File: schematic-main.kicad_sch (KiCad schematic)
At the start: 10 parts, among them J1 Conn_01x02, J2 Conn_01x03, J3 Conn_01x02, J6 Conn_01x04, P1 USB_C_Plug_USB2.0

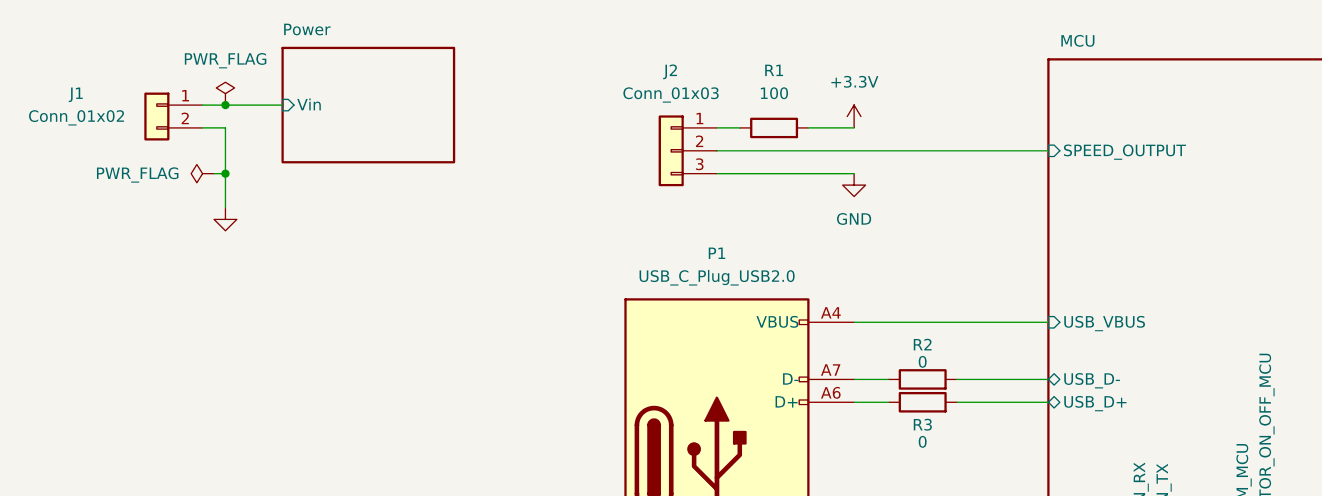
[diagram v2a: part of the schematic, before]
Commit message: Add Schottky Diode for VBUS and Vreg
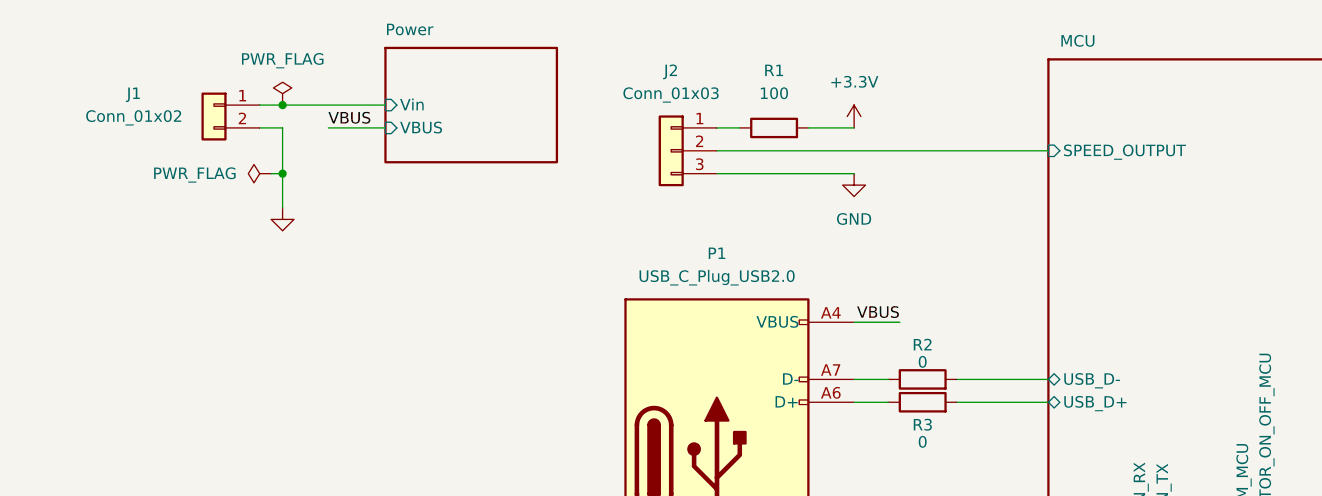
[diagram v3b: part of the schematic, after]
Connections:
- net MCU/USB_VBUS renamed VBUS
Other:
- sheet MCU ports: added none; removed USB_VBUS
- sheet Power  ports: added VBUS; removed none
- moved on the sheet: J1
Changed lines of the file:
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@@
   (junction (at 97.79 96.52) (diameter 0) (color 0 0 0 0)
   )
-  (junction (at 43.18 33.02) (diameter 0) (color 0 0 0 0)
-  )
-  (junction (at 43.18 40.64) (diameter 0) (color 0 0 0 0)
+  (junction (at 49.53 33.02) (diameter 0) (color 0 0 0 0)
+  )
+  (junction (at 49.53 40.64) (diameter 0) (color 0 0 0 0)
   )
   (junction (at 115.57 96.52) (diameter 0) (color 0 0 0 0)
@@
     (stroke (width 0) (type default))
   )
-  (wire (pts (xy 40.64 33.02) (xy 43.18 33.02))
+  (wire (pts (xy 118.11 57.15) (xy 113.03 57.15))
+    (stroke (width 0) (type default))
+  )
+  (wire (pts (xy 46.99 33.02) (xy 49.53 33.02))
     (stroke (width 0) (type default))
   )
@@
     (stroke (width 0) (type default))
   )
+  (wire (pts (xy 54.61 35.56) (xy 60.96 35.56))
+    (stroke (width 0) (type default))
+  )
   (wire (pts (xy 130.81 147.32) (xy 115.57 147.32))
     (stroke (width 0) (type default))
@@
     (stroke (width 0) (type default))
   )
-  (wire (pts (xy 43.18 40.64) (xy 43.18 44.45))
+  (wire (pts (xy 49.53 40.64) (xy 49.53 44.45))
     (stroke (width 0) (type default))
   )
@@
     (stroke (width 0) (type default))
   )
-  (wire (pts (xy 113.03 57.15) (xy 134.62 57.15))
-    (stroke (width 0) (type default))
-  )
   (wire (pts (xy 123.19 96.52) (xy 123.19 95.25))
     (stroke (width 0) (type default))
@@
     (stroke (width 0) (type default))
   )
-  (wire (pts (xy 40.64 35.56) (xy 43.18 35.56))
+  (wire (pts (xy 46.99 35.56) (xy 49.53 35.56))
     (stroke (width 0) (type default))
   )
@@
     (stroke (width 0) (type default))
   )
-  (wire (pts (xy 43.18 35.56) (xy 43.18 40.64))
+  (wire (pts (xy 49.53 35.56) (xy 49.53 40.64))
     (stroke (width 0) (type default))
   )
@@
     (stroke (width 0) (type default))
   )
-  (wire (pts (xy 43.18 33.02) (xy 49.53 33.02))
+  (wire (pts (xy 49.53 33.02) (xy 60.96 33.02))
     (stroke (width 0) (type default))
   )
@@
     (stroke (width 0) (type default))
   )
-  (wire (pts (xy 41.91 40.64) (xy 43.18 40.64))
+  (wire (pts (xy 48.26 40.64) (xy 49.53 40.64))
     (stroke (width 0) (type default))
   )
@@
   )
   (label "MOTOR_ON_OFF" (at 194.31 147.32 180) (fields_autoplaced)
+    (effects (font (size 1.27 1.27)) (justify right bottom))
+  )
+  (label "VBUS" (at 54.61 35.56 0) (fields_autoplaced)
+    (effects (font (size 1.27 1.27)) (justify left bottom))
+  )
+  (label "VBUS" (at 118.11 57.15 180) (fields_autoplaced)
     (effects (font (size 1.27 1.27)) (justify right bottom))
   )
@@
     )
   )
-  (symbol (lib_id "power:GND") (at 43.18 44.45 0) (unit 1)
-    (in_bom yes) (on_board yes) (dnp no) (fields_autoplaced)
-    (property "Reference" "#PWR03" (at 43.18 50.8 0)
-      (effects (font (size 1.27 1.27)) hide)
-    )
-    (property "Value" "GND" (at 43.18 49.53 0)
-      (effects (font (size 1.27 1.27)) hide)
-    )
-    (property "Footprint" "" (at 43.18 44.45 0)
-      (effects (font (size 1.27 1.27)) hide)
-    )
-    (property "Datasheet" "" (at 43.18 44.45 0)
+  (symbol (lib_id "power:GND") (at 49.53 44.45 0) (unit 1)
+    (in_bom yes) (on_board yes) (dnp no) (fields_autoplaced)
+    (property "Reference" "#PWR03" (at 49.53 50.8 0)
+      (effects (font (size 1.27 1.27)) hide)
+    )
+    (property "Value" "GND" (at 49.53 49.53 0)
+      (effects (font (size 1.27 1.27)) hide)
+    )
+    (property "Footprint" "" (at 49.53 44.45 0)
+      (effects (font (size 1.27 1.27)) hide)
+    )
+    (property "Datasheet" "" (at 49.53 44.45 0)
       (effects (font (size 1.27 1.27)) hide)
     )
@@
     )
   )
-  (symbol (lib_id "Connector_Generic:Conn_01x02") (at 35.56 33.02 0) (mirror y) (unit 1)
+  (symbol (lib_id "Connector_Generic:Conn_01x02") (at 41.91 33.02 0) (mirror y) (unit 1)
     (in_bom yes) (on_board yes) (dnp no)
-    (property "Reference" "J1" (at 26.67 31.75 0)
-      (effects (font (size 1.27 1.27)))
-    )
-    (property "Value" "Conn_01x02" (at 26.67 34.29 0)
-      (effects (font (size 1.27 1.27)))
-    )
-    (property "Footprint" "" (at 35.56 33.02 0)
-      (effects (font (size 1.27 1.27)) hide)
-    )
-    (property "Datasheet" "~" (at 35.56 33.02 0)
+    (property "Reference" "J1" (at 33.02 31.75 0)
+      (effects (font (size 1.27 1.27)))
+    )
+    (property "Value" "Conn_01x02" (at 33.02 34.29 0)
+      (effects (font (size 1.27 1.27)))
+    )
+    (property "Footprint" "" (at 41.91 33.02 0)
+      (effects (font (size 1.27 1.27)) hide)
+    )
+    (property "Datasheet" "~" (at 41.91 33.02 0)
       (effects (font (size 1.27 1.27)) hide)
     )
@@
       (effects (font (size 1.27 1.27)) hide)
     )
+    (pin "1")
+    (pin "2")
     (pin "3")
-    (pin "1")
     (pin "4")
-    (pin "2")
     (instances
       (project "schematic-main"
@@
     )
   )
-  (symbol (lib_id "power:PWR_FLAG") (at 41.91 40.64 90) (unit 1)
-    (in_bom yes) (on_board yes) (dnp no) (fields_autoplaced)
-    (property "Reference" "#FLG02" (at 40.005 40.64 0)
-      (effects (font (size 1.27 1.27)) hide)
-    )
-    (property "Value" "PWR_FLAG" (at 38.1 40.64 90)
-      (effects (font (size 1.27 1.27)) (justify left))
-    )
-    (property "Footprint" "" (at 41.91 40.64 0)
-      (effects (font (size 1.27 1.27)) hide)
-    )
-    (property "Datasheet" "~" (at 41.91 40.64 0)
+  (symbol (lib_id "power:PWR_FLAG") (at 48.26 40.64 90) (unit 1)
+    (in_bom yes) (on_board yes) (dnp no) (fields_autoplaced)
+    (property "Reference" "#FLG02" (at 46.355 40.64 0)
+      (effects (font (size 1.27 1.27)) hide)
+    )
+    (property "Value" "PWR_FLAG" (at 44.45 40.64 90)
+      (effects (font (size 1.27 1.27)) (justify left))
+    )
+    (property "Footprint" "" (at 48.26 40.64 0)
+      (effects (font (size 1.27 1.27)) hide)
+    )
+    (property "Datasheet" "~" (at 48.26 40.64 0)
       (effects (font (size 1.27 1.27)) hide)
     )
@@
     )
     (pin "1")
+    (pin "2")
     (pin "3")
-    (pin "2")
     (instances
       (project "schematic-main"
@@
     )
   )
-  (symbol (lib_id "power:PWR_FLAG") (at 43.18 33.02 0) (unit 1)
-    (in_bom yes) (on_board yes) (dnp no) (fields_autoplaced)
-    (property "Reference" "#FLG01" (at 43.18 31.115 0)
-      (effects (font (size 1.27 1.27)) hide)
-    )
-    (property "Value" "PWR_FLAG" (at 43.18 27.94 0)
-      (effects (font (size 1.27 1.27)))
-    )
-    (property "Footprint" "" (at 43.18 33.02 0)
-      (effects (font (size 1.27 1.27)) hide)
-    )
-    (property "Datasheet" "~" (at 43.18 33.02 0)
+  (symbol (lib_id "power:PWR_FLAG") (at 49.53 33.02 0) (unit 1)
+    (in_bom yes) (on_board yes) (dnp no) (fields_autoplaced)
+    (property "Reference" "#FLG01" (at 49.53 31.115 0)
+      (effects (font (size 1.27 1.27)) hide)
+    )
+    (property "Value" "PWR_FLAG" (at 49.53 27.94 0)
+      (effects (font (size 1.27 1.27)))
+    )
+    (property "Footprint" "" (at 49.53 33.02 0)
+      (effects (font (size 1.27 1.27)) hide)
+    )
+    (property "Datasheet" "~" (at 49.53 33.02 0)
       (effects (font (size 1.27 1.27)) hide)
     )
@@
     )
   )
-  (sheet (at 49.53 26.67) (size 19.05 12.7)
+  (sheet (at 60.96 26.67) (size 19.05 12.7)
     (stroke (width 0.254) (type solid))
     (fill (color 255 255 154 1.0000))
-    (property "Sheetname" "Power " (at 49.53 25.4 0)
+    (property "Sheetname" "Power " (at 60.96 25.4 0)
       (effects (font (size 1.27 1.27)) (justify left bottom))
     )
-    (property "Sheetfile" "schematic-power.kicad_sch" (at 50.8 47.625 0)
+    (property "Sheetfile" "schematic-power.kicad_sch" (at 62.23 47.625 0)
       (effects (font (size 1.27 1.27)) (justify left top) hide)
     )
-    (pin "Vin" input (at 49.53 33.02 180)
+    (pin "Vin" input (at 60.96 33.02 180)
+      (effects (font (size 1.27 1.27)) (justify left))
+    )
+    (pin "VBUS" input (at 60.96 35.56 180)
       (effects (font (size 1.27 1.27)) (justify left))
     )
@@
       (effects (font (size 1.27 1.27)) (justify left))
     )
-    (pin "USB_VBUS" input (at 134.62 57.15 180)
-      (effects (font (size 1.27 1.27)) (justify left))
-    )

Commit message: PCB Drawing
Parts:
- added H1, H2, H3, H4: MountingHole, MountingHole:MountingHole_2.2mm_M2, symbol Mechanical:MountingHole
- J1, J3: footprint (none) -> Connector_PinHeader_1.00mm:PinHeader_1x02_P1.00mm_Vertical
- J2: footprint (none) -> Connector_PinHeader_1.00mm:PinHeader_1x03_P1.00mm_Vertical
- J6: footprint (none) -> Connector_PinHeader_1.00mm:PinHeader_1x04_P1.00mm_Vertical
- P1: footprint (none) -> Connector_USB:2169900002
- R1, R2, R3, R4, R5: footprint (none) -> Resistor_SMD:R_1206_3216Metric
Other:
- note added: "Mounting Holes"
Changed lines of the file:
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@@
     (stroke (width 0) (type default))
+  )
+  (rectangle (start 34.29 102.87) (end 55.88 130.81)
+    (stroke (width 0) (type dash))
+    (fill (type none))
+  )
+  (text "Mounting Holes" (at 34.29 101.6 0)
+    (effects (font (size 1.7 1.7) (thickness 0.4) bold) (justify left bottom))
   )
   (label "PWM_MOTOR" (at 130.81 144.78 180) (fields_autoplaced)
@@
       (effects (font (size 1.27 1.27)))
     )
-    (property "Footprint" "" (at 101.6 72.39 0)
+    (property "Footprint" "Connector_USB:2169900002" (at 101.6 72.39 0)
       (effects (font (size 1.27 1.27)) hide)
     )
@@
       (effects (font (size 1.27 1.27)))
     )
-    (property "Footprint" "" (at 110.49 125.73 0)
+    (property "Footprint" "Connector_PinHeader_1.00mm:PinHeader_1x02_P1.00mm_Vertical" (at 110.49 125.73 0)
       (effects (font (size 1.27 1.27)) hide)
     )
@@
       (effects (font (size 1.27 1.27)))
     )
-    (property "Footprint" "" (at 41.91 33.02 0)
+    (property "Footprint" "Connector_PinHeader_1.00mm:PinHeader_1x02_P1.00mm_Vertical" (at 41.91 33.02 0)
       (effects (font (size 1.27 1.27)) hide)
     )
@@
       (effects (font (size 1.27 1.27)))
     )
-    (property "Footprint" "" (at 120.65 67.818 90)
+    (property "Footprint" "Resistor_SMD:R_1206_3216Metric" (at 120.65 67.818 90)
       (effects (font (size 1.27 1.27)) hide)
     )
@@
       (effects (font (size 1.27 1.27)))
     )
-    (property "Footprint" "" (at 110.49 144.78 0)
+    (property "Footprint" "Connector_PinHeader_1.00mm:PinHeader_1x04_P1.00mm_Vertical" (at 110.49 144.78 0)
       (effects (font (size 1.27 1.27)) hide)
     )
@@
       (effects (font (size 1.27 1.27)))
     )
-    (property "Footprint" "" (at 104.14 37.338 90)
+    (property "Footprint" "Resistor_SMD:R_1206_3216Metric" (at 104.14 37.338 90)
       (effects (font (size 1.27 1.27)) hide)
     )
@@
         (path "/c9ad7189-d3b2-414a-9743-efd8e57cd755"
           (reference "R1") (unit 1)
+        )
+      )
+    )
+  )
+  (symbol (lib_id "Mechanical:MountingHole") (at 38.1 113.03 0) (unit 1)
+    (in_bom yes) (on_board yes) (dnp no) (fields_autoplaced)
+    (property "Reference" "H2" (at 40.64 111.76 0)
+      (effects (font (size 1.27 1.27)) (justify left))
+    )
+    (property "Value" "MountingHole" (at 40.64 114.3 0)
+      (effects (font (size 1.27 1.27)) (justify left))
+    )
+    (property "Footprint" "MountingHole:MountingHole_2.2mm_M2" (at 38.1 113.03 0)
+      (effects (font (size 1.27 1.27)) hide)
+    )
+    (property "Datasheet" "~" (at 38.1 113.03 0)
+      (effects (font (size 1.27 1.27)) hide)
+    )
+    (instances
+      (project "schematic-main"
+        (path "/c9ad7189-d3b2-414a-9743-efd8e57cd755"
+          (reference "H2") (unit 1)
         )
       )
@@
       (effects (font (size 1.27 1.27)))
     )
-    (property "Footprint" "" (at 120.65 65.278 90)
+    (property "Footprint" "Resistor_SMD:R_1206_3216Metric" (at 120.65 65.278 90)
       (effects (font (size 1.27 1.27)) hide)
     )
@@
     )
   )
+  (symbol (lib_id "Mechanical:MountingHole") (at 38.1 106.68 0) (unit 1)
+    (in_bom yes) (on_board yes) (dnp no) (fields_autoplaced)
+    (property "Reference" "H1" (at 40.64 105.41 0)
+      (effects (font (size 1.27 1.27)) (justify left))
+    )
+    (property "Value" "MountingHole" (at 40.64 107.95 0)
+      (effects (font (size 1.27 1.27)) (justify left))
+    )
+    (property "Footprint" "MountingHole:MountingHole_2.2mm_M2" (at 38.1 106.68 0)
+      (effects (font (size 1.27 1.27)) hide)
+    )
+    (property "Datasheet" "~" (at 38.1 106.68 0)
+      (effects (font (size 1.27 1.27)) hide)
+    )
+    (instances
+      (project "schematic-main"
+        (path "/c9ad7189-d3b2-414a-9743-efd8e57cd755"
+          (reference "H1") (unit 1)
+        )
+      )
+    )
+  )
   (symbol (lib_id "power:GND") (at 106.68 96.52 0) (unit 1)
     (in_bom yes) (on_board yes) (dnp no) (fields_autoplaced)
@@
       (effects (font (size 1.27 1.27)))
     )
-    (property "Footprint" "" (at 92.71 38.1 0)
+    (property "Footprint" "Connector_PinHeader_1.00mm:PinHeader_1x03_P1.00mm_Vertical" (at 92.71 38.1 0)
       (effects (font (size 1.27 1.27)) hide)
     )
@@
     )
   )
+  (symbol (lib_id "Mechanical:MountingHole") (at 38.1 125.73 0) (unit 1)
+    (in_bom yes) (on_board yes) (dnp no) (fields_autoplaced)
+    (property "Reference" "H4" (at 40.64 124.46 0)
+      (effects (font (size 1.27 1.27)) (justify left))
+    )
+    (property "Value" "MountingHole" (at 40.64 127 0)
+      (effects (font (size 1.27 1.27)) (justify left))
+    )
+    (property "Footprint" "MountingHole:MountingHole_2.2mm_M2" (at 38.1 125.73 0)
+      (effects (font (size 1.27 1.27)) hide)
+    )
+    (property "Datasheet" "~" (at 38.1 125.73 0)
+      (effects (font (size 1.27 1.27)) hide)
+    )
+    (instances
+      (project "schematic-main"
+        (path "/c9ad7189-d3b2-414a-9743-efd8e57cd755"
+          (reference "H4") (unit 1)
+        )
+      )
+    )
+  )
   (symbol (lib_id "Device:R") (at 115.57 91.44 0) (unit 1)
     (in_bom yes) (on_board yes) (dnp no) (fields_autoplaced)
@@
       (effects (font (size 1.27 1.27)) (justify left))
     )
-    (property "Footprint" "" (at 113.792 91.44 90)
+    (property "Footprint" "Resistor_SMD:R_1206_3216Metric" (at 113.792 91.44 90)
       (effects (font (size 1.27 1.27)) hide)
     )
@@
       (effects (font (size 1.27 1.27)) (justify left))
     )
-    (property "Footprint" "" (at 121.412 91.44 90)
+    (property "Footprint" "Resistor_SMD:R_1206_3216Metric" (at 121.412 91.44 90)
       (effects (font (size 1.27 1.27)) hide)
     )
@@
         )
       )
+    )
+  )
+  (symbol (lib_id "Mechanical:MountingHole") (at 38.1 119.38 0) (unit 1)
+    (in_bom yes) (on_board yes) (dnp no) (fields_autoplaced)
+    (property "Reference" "H3" (at 40.64 118.11 0)
+      (effects (font (size 1.27 1.27)) (justify left))
+    )
+    (property "Value" "MountingHole" (at 40.64 120.65 0)
+      (effects (font (size 1.27 1.27)) (justify left))
+    )
+    (property "Footprint" "MountingHole:MountingHole_2.2mm_M2" (at 38.1 119.38 0)
+      (effects (font (size 1.27 1.27)) hide)
+    )
+    (property "Datasheet" "~" (at 38.1 119.38 0)
+      (effects (font (size 1.27 1.27)) hide)
+    )
+    (instances
+      (project "schematic-main"
+        (path "/c9ad7189-d3b2-414a-9743-efd8e57cd755"
+          (reference "H3") (unit 1)
+        )
+      )

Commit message: Add Molex, change of layout for CAN and Optocouplers
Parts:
- J1, J3: footprint Connector_PinHeader_1.00mm:PinHeader_1x02_P1.00mm_Vertical -> Connector_Molex:Molex_Mini-Fit_Jr_5569-02A2_2x01_P4.20mm_Horizontal
- J2: footprint Connector_PinHeader_1.00mm:PinHeader_1x03_P1.00mm_Vertical -> Connector_Molex:Molex_Mini-Fit_Jr_5569-04A2_2x02_P4.20mm_Horizontal
- J6: footprint Connector_PinHeader_1.00mm:PinHeader_1x04_P1.00mm_Vertical -> Connector_Molex:Molex_Mini-Fit_Jr_5569-04A2_2x02_P4.20mm_Horizontal
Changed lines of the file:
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@@
       (effects (font (size 1.27 1.27)))
     )
-    (property "Footprint" "Connector_PinHeader_1.00mm:PinHeader_1x02_P1.00mm_Vertical" (at 110.49 125.73 0)
+    (property "Footprint" "Connector_Molex:Molex_Mini-Fit_Jr_5569-02A2_2x01_P4.20mm_Horizontal" (at 110.49 125.73 0)
       (effects (font (size 1.27 1.27)) hide)
     )
@@
       (effects (font (size 1.27 1.27)))
     )
-    (property "Footprint" "Connector_PinHeader_1.00mm:PinHeader_1x02_P1.00mm_Vertical" (at 41.91 33.02 0)
+    (property "Footprint" "Connector_Molex:Molex_Mini-Fit_Jr_5569-02A2_2x01_P4.20mm_Horizontal" (at 41.91 33.02 0)
       (effects (font (size 1.27 1.27)) hide)
     )
@@
       (effects (font (size 1.27 1.27)))
     )
-    (property "Footprint" "Connector_PinHeader_1.00mm:PinHeader_1x04_P1.00mm_Vertical" (at 110.49 144.78 0)
+    (property "Footprint" "Connector_Molex:Molex_Mini-Fit_Jr_5569-04A2_2x02_P4.20mm_Horizontal" (at 110.49 144.78 0)
       (effects (font (size 1.27 1.27)) hide)
     )
@@
       (effects (font (size 1.27 1.27)))
     )
-    (property "Footprint" "Connector_PinHeader_1.00mm:PinHeader_1x03_P1.00mm_Vertical" (at 92.71 38.1 0)
-      (effects (font (size 1.27 1.27)) hide)
-    )
+    (property "Footprint" "Connector_Molex:Molex_Mini-Fit_Jr_5569-04A2_2x02_P4.20mm_Horizontal" (at 92.71 38.1 0)
+      (effects (font (size 1.27 1.27)) hide)
+    )

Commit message: Adding library and fixing errors related to the ideal diode
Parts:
- J1, J3: footprint Connector_Molex:Molex_Mini-Fit_Jr_5569-02A2_2x01_P4.20mm_Horizontal -> Connector_Molex:39-30-102Y
- J2, J6: footprint Connector_Molex:Molex_Mini-Fit_Jr_5569-04A2_2x02_P4.20mm_Horizontal -> Connector_Molex:39-30-104Y
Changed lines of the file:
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@@
       (effects (font (size 1.27 1.27)))
     )
-    (property "Footprint" "Connector_Molex:Molex_Mini-Fit_Jr_5569-02A2_2x01_P4.20mm_Horizontal" (at 110.49 125.73 0)
+    (property "Footprint" "Connector_Molex:39-30-102Y" (at 110.49 125.73 0)
       (effects (font (size 1.27 1.27)) hide)
     )
@@
       (effects (font (size 1.27 1.27)))
     )
-    (property "Footprint" "Connector_Molex:Molex_Mini-Fit_Jr_5569-02A2_2x01_P4.20mm_Horizontal" (at 41.91 33.02 0)
+    (property "Footprint" "Connector_Molex:39-30-102Y" (at 41.91 33.02 0)
       (effects (font (size 1.27 1.27)) hide)
     )
@@
       (effects (font (size 1.27 1.27)))
     )
-    (property "Footprint" "Connector_Molex:Molex_Mini-Fit_Jr_5569-04A2_2x02_P4.20mm_Horizontal" (at 110.49 144.78 0)
+    (property "Footprint" "Connector_Molex:39-30-104Y" (at 110.49 144.78 0)
       (effects (font (size 1.27 1.27)) hide)
     )
@@
       (effects (font (size 1.27 1.27)))
     )
-    (property "Footprint" "Connector_Molex:Molex_Mini-Fit_Jr_5569-04A2_2x02_P4.20mm_Horizontal" (at 92.71 38.1 0)
-      (effects (font (size 1.27 1.27)) hide)
-    )
+    (property "Footprint" "Connector_Molex:39-30-104Y" (at 92.71 38.1 0)
+      (effects (font (size 1.27 1.27)) hide)
+    )
